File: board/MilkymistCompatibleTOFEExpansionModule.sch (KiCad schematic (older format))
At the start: 115 parts, among them CON1 AUDIO_JACK_3535NG, CON2 AUDIO_JACK_3535NG, CON3 AUDIO_JACK_3535NG, CON4 AUDIO_JACK_3535NG, IC1 PC817, J1 DB9, K1 CONN_2, K2 CONN_2, K3 CONN_3, K4 CONN_3, K5 CONN_2, K6 CONN_2, K7 CONN_2, K8 CONN_2, P2 CONN_4X2, P4 CONN_6X2, P5 CONN_6X2, Q1 TRANSISTOR-NPN, SW1 SW_PUSH, SW2 SW_PUSH, SW3 SW_PUSH, SW4 SW_PUSH, U1 LM4550, U2 7805_N, U3 ST3232CDR, U4 SN74LVC1G17, U5 ISL83490, U6 IR-RX, U7 24AA01/24LC01B, U8 TIMVIDEOS-PCIE-8X, X1 CRYSTAL

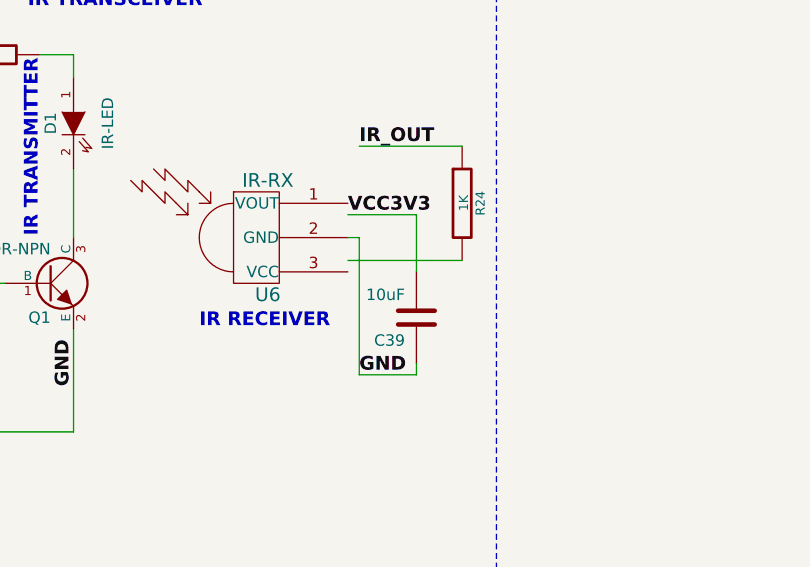
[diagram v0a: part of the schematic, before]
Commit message: Mechanical hole changes
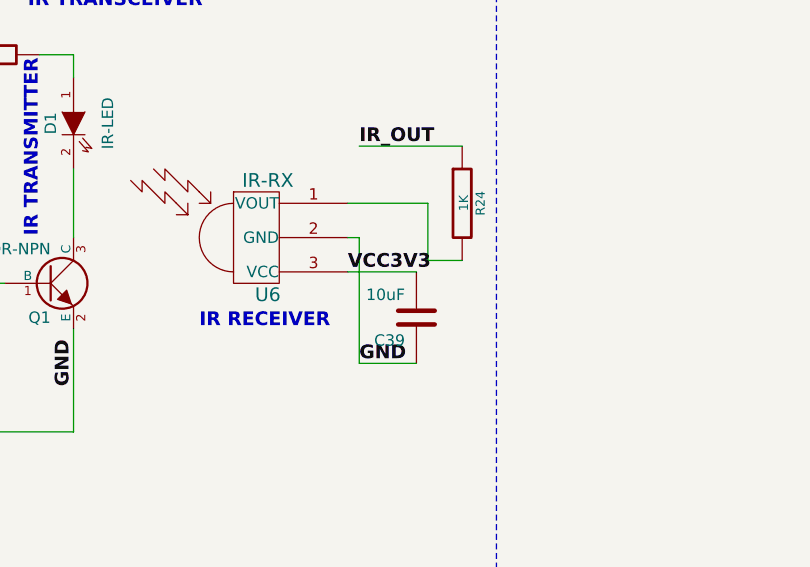
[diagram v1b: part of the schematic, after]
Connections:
- net VCC3V3: now also U6.3 (VCC)
- net at R24.2: now also U6.1 (VOUT)
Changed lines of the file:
@@
 Sheet 1 1
 Title "Milkymist Compatible TOFE Expansion Module"
-Date "2 nov 2015"
+Date "2 dec 2015"
 Rev "1.0"
 Comp "Numato Lab"
@@
 	-1   0    0    1
 $EndComp
-Wire Wire Line
-	18050 13750 18350 13750
-Wire Wire Line
-	18350 13750 18350 14000
-Text Label 18050 13750 0    60   ~ 12
+Text Label 18050 14000 0    60   ~ 12
 VCC3V3
-Wire Wire Line
-	18050 13850 18100 13850
-Wire Wire Line
-	18100 13850 18100 14450
-Wire Wire Line
-	18100 14450 18350 14450
-Wire Wire Line
-	18350 14450 18350 14400
-Text Label 18100 14450 0    60   ~ 12
+Text Label 18100 14400 0    60   ~ 12
 GND
-Wire Wire Line
-	18050 13950 18550 13950
 Wire Wire Line
 	18550 13450 18100 13450
@@
 NoConn ~ 16450 5500
 NoConn ~ 16450 4000
+Wire Wire Line
+	18050 14000 18350 14000
+Wire Wire Line
+	18050 13850 18100 13850
+Wire Wire Line
+	18100 13850 18100 14400
+Wire Wire Line
+	18100 14400 18350 14400
+Wire Wire Line
+	18050 13700 18400 13700
+Wire Wire Line
+	18400 13700 18400 13950
+Wire Wire Line
+	18400 13950 18550 13950
 $EndSCHEMATC
